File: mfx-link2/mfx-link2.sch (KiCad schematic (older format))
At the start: 48 parts, among them P1 CONN_01X04, P2 Gleisbox, P4 UART, P5 I2C, P6 CONN_02X03, P7 POTI, P8 IBT-2, Q1 BC817-40, T1 53040C, U1 6N137, U2 7805, U3 LM393, U4 78L05, U5 PIC16F1709

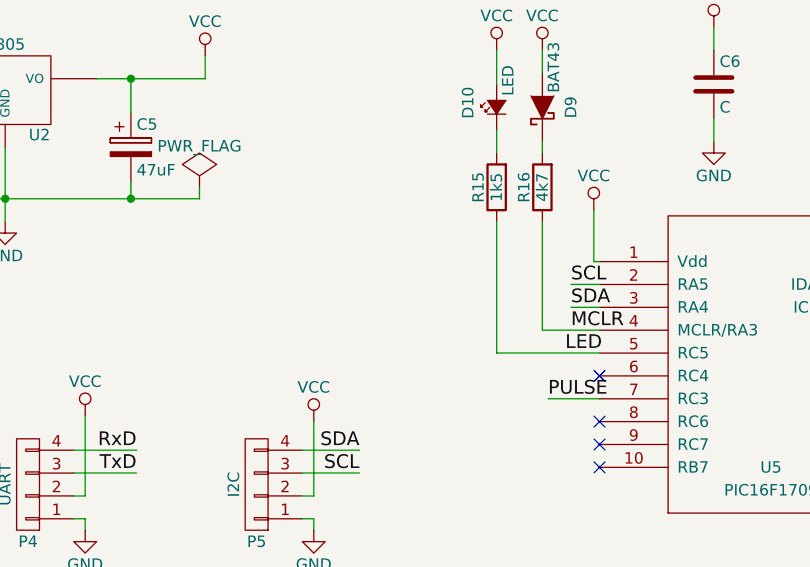
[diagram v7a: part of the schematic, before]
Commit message: add switch button
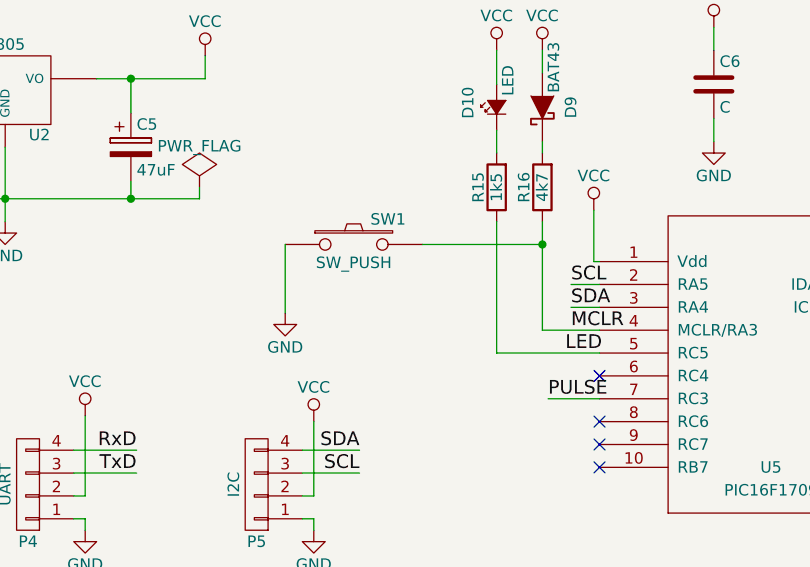
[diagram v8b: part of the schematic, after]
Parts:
- added SW1: SW_PUSH, w_switch:PCB_PUSH, symbol SW_PUSH
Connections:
- net GND: now also SW1.1
- net MCLR: now also SW1.2
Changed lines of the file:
@@
 EESchema Schematic File Version 2
+LIBS:mfx-link2-rescue
 LIBS:power
 LIBS:device
@@
 $EndComp
 $Comp
-L PWR_FLAG #FLG01
+L PWR_FLAG #FLG2
 U 1 1 58FE3ABA
 P 4950 1775
-F 0 "#FLG01" H 4950 1870 50  0001 C CNN
+F 0 "#FLG2" H 4950 1870 50  0001 C CNN
 F 1 "PWR_FLAG" H 4950 1955 50  0000 C CNN
 F 2 "" H 4950 1775 50  0000 C CNN
@@
 $EndComp
 $Comp
-L +5V #PWR02
+L +5V #PWR5
 U 1 1 58FE4D35
 P 3950 6350
-F 0 "#PWR02" H 3950 6200 50  0001 C CNN
+F 0 "#PWR5" H 3950 6200 50  0001 C CNN
 F 1 "+5V" H 3950 6490 50  0000 C CNN
 F 2 "" H 3950 6350 50  0000 C CNN
@@
 ENABLE
 $Comp
-L GND #PWR03
+L GND #PWR27
 U 1 1 58FE66BD
 P 10325 3075
-F 0 "#PWR03" H 10325 2825 50  0001 C CNN
+F 0 "#PWR27" H 10325 2825 50  0001 C CNN
 F 1 "GND" H 10325 2925 50  0000 C CNN
 F 2 "" H 10325 3075 50  0000 C CNN
@@
 SENSE
 $Comp
-L GND #PWR04
+L GND #PWR22
 U 1 1 58FE942D
 P 8475 2200
-F 0 "#PWR04" H 8475 1950 50  0001 C CNN
+F 0 "#PWR22" H 8475 1950 50  0001 C CNN
 F 1 "GND" H 8475 2050 50  0000 C CNN
 F 2 "" H 8475 2200 50  0000 C CNN
@@
 $EndComp
 $Comp
-L GND #PWR05
+L GND #PWR24
 U 1 1 58FFB153
 P 8750 1925
-F 0 "#PWR05" H 8750 1675 50  0001 C CNN
+F 0 "#PWR24" H 8750 1675 50  0001 C CNN
 F 1 "GND" H 8750 1775 50  0000 C CNN
 F 2 "" H 8750 1925 50  0000 C CNN
@@
 _GB_OUT
 $Comp
-L GNDA #PWR06
+L GNDA #PWR16
 U 1 1 59001DF4
 P 5625 7000
-F 0 "#PWR06" H 5625 6750 50  0001 C CNN
+F 0 "#PWR16" H 5625 6750 50  0001 C CNN
 F 1 "GNDA" H 5625 6850 50  0000 C CNN
 F 2 "" H 5625 7000 50  0000 C CNN
@@
 $EndComp
 $Comp
-L +5V #PWR07
+L +5V #PWR11
 U 1 1 5909C148
 P 4650 4825
-F 0 "#PWR07" H 4650 4675 50  0001 C CNN
+F 0 "#PWR11" H 4650 4675 50  0001 C CNN
 F 1 "+5V" H 4650 4965 50  0000 C CNN
 F 2 "" H 4650 4825 50  0000 C CNN
@@
 $EndComp
 $Comp
-L PWR_FLAG #FLG08
+L PWR_FLAG #FLG1
 U 1 1 590A0357
 P 3375 5550
-F 0 "#FLG08" H 3375 5645 50  0001 C CNN
+F 0 "#FLG1" H 3375 5645 50  0001 C CNN
 F 1 "PWR_FLAG" H 3375 5730 50  0000 C CNN
 F 2 "" H 3375 5550 50  0000 C CNN
@@
 red
 $Comp
-L +5V #PWR09
+L +5V #PWR3
 U 1 1 5908A86E
 P 3525 6075
-F 0 "#PWR09" H 3525 5925 50  0001 C CNN
+F 0 "#PWR3" H 3525 5925 50  0001 C CNN
 F 1 "+5V" H 3525 6215 50  0000 C CNN
 F 2 "" H 3525 6075 50  0000 C CNN
@@
 $EndComp
 $Comp
-L GND #PWR010
+L GND #PWR7
 U 1 1 58FE372A
 P 4100 1925
-F 0 "#PWR010" H 4100 1675 50  0001 C CNN
+F 0 "#PWR7" H 4100 1675 50  0001 C CNN
 F 1 "GND" H 4100 1775 50  0000 C CNN
 F 2 "" H 4100 1925 50  0000 C CNN
@@
 $EndComp
 $Comp
-L GND #PWR011
+L GND #PWR21
 U 1 1 58FE38A1
 P 7200 1575
-F 0 "#PWR011" H 7200 1325 50  0001 C CNN
+F 0 "#PWR21" H 7200 1325 50  0001 C CNN
 F 1 "GND" H 7200 1425 50  0000 C CNN
 F 2 "" H 7200 1575 50  0000 C CNN
@@
 $EndComp
 $Comp
-L GND #PWR012
+L GND #PWR15
 U 1 1 58FF775E
 P 5450 3275
-F 0 "#PWR012" H 5450 3025 50  0001 C CNN
+F 0 "#PWR15" H 5450 3025 50  0001 C CNN
 F 1 "GND" H 5450 3125 50  0000 C CNN
 F 2 "" H 5450 3275 50  0000 C CNN
@@
 $EndComp
 $Comp
-L GND #PWR013
+L GND #PWR10
 U 1 1 58FF8516
 P 4450 3275
-F 0 "#PWR013" H 4450 3025 50  0001 C CNN
+F 0 "#PWR10" H 4450 3025 50  0001 C CNN
 F 1 "GND" H 4450 3125 50  0000 C CNN
 F 2 "" H 4450 3275 50  0000 C CNN
@@
 $EndComp
 $Comp
-L GND #PWR014
+L GND #PWR2
 U 1 1 5909205E
 P 3100 3300
-F 0 "#PWR014" H 3100 3050 50  0001 C CNN
+F 0 "#PWR2" H 3100 3050 50  0001 C CNN
 F 1 "GND" H 3100 3150 50  0000 C CNN
 F 2 "" H 3100 3300 50  0000 C CNN
@@
 $EndComp
 $Comp
-L GNDA #PWR015
+L GNDA #PWR6
 U 1 1 59092D00
 P 3950 7150
-F 0 "#PWR015" H 3950 6900 50  0001 C CNN
+F 0 "#PWR6" H 3950 6900 50  0001 C CNN
 F 1 "GNDA" H 3950 7000 50  0000 C CNN
 F 2 "" H 3950 7150 50  0000 C CNN
@@
 $EndComp
 $Comp
-L GNDA #PWR016
+L GNDA #PWR4
 U 1 1 59092E5B
 P 3525 7425
-F 0 "#PWR016" H 3525 7175 50  0001 C CNN
+F 0 "#PWR4" H 3525 7175 50  0001 C CNN
 F 1 "GNDA" H 3525 7275 50  0000 C CNN
 F 2 "" H 3525 7425 50  0000 C CNN
@@
 $EndComp
 $Comp
-L GNDA #PWR017
+L GNDA #PWR8
 U 1 1 590931B4
 P 4150 5750
-F 0 "#PWR017" H 4150 5500 50  0001 C CNN
+F 0 "#PWR8" H 4150 5500 50  0001 C CNN
 F 1 "GNDA" H 4150 5600 50  0000 C CNN
 F 2 "" H 4150 5750 50  0000 C CNN
@@
 $EndComp
 $Comp
-L VCC #PWR018
+L VCC #PWR12
 U 1 1 59094284
 P 4975 1200
-F 0 "#PWR018" H 4975 1050 50  0001 C CNN
+F 0 "#PWR12" H 4975 1050 50  0001 C CNN
 F 1 "VCC" H 4975 1350 50  0000 C CNN
 F 2 "" H 4975 1200 50  0000 C CNN
@@
 $EndComp
 $Comp
-L VCC #PWR019
+L VCC #PWR20
 U 1 1 590943B0
 P 7200 1075
-F 0 "#PWR019" H 7200 925 50  0001 C CNN
+F 0 "#PWR20" H 7200 925 50  0001 C CNN
 F 1 "VCC" H 7200 1225 50  0000 C CNN
 F 2 "" H 7200 1075 50  0000 C CNN
@@
 $EndComp
 $Comp
-L VCC #PWR020
+L VCC #PWR17
 U 1 1 590944D7
 P 6250 1175
-F 0 "#PWR020" H 6250 1025 50  0001 C CNN
+F 0 "#PWR17" H 6250 1025 50  0001 C CNN
 F 1 "VCC" H 6250 1325 50  0000 C CNN
 F 2 "" H 6250 1175 50  0000 C CNN
@@
 $EndComp
 $Comp
-L VCC #PWR021
+L VCC #PWR18
 U 1 1 5909459E
 P 6450 1175
-F 0 "#PWR021" H 6450 1025 50  0001 C CNN
+F 0 "#PWR18" H 6450 1025 50  0001 C CNN
 F 1 "VCC" H 6450 1325 50  0000 C CNN
 F 2 "" H 6450 1175 50  0000 C CNN
@@
 $EndComp
 $Comp
-L VCC #PWR022
+L VCC #PWR19
 U 1 1 5909516C
 P 6675 1875
-F 0 "#PWR022" H 6675 1725 50  0001 C CNN
+F 0 "#PWR19" H 6675 1725 50  0001 C CNN
 F 1 "VCC" H 6675 2025 50  0000 C CNN
 F 2 "" H 6675 1875 50  0000 C CNN
@@
 $EndComp
 $Comp
-L VCC #PWR023
+L VCC #PWR1
 U 1 1 5909A87E
 P 3000 2425
-F 0 "#PWR023" H 3000 2275 50  0001 C CNN
+F 0 "#PWR1" H 3000 2275 50  0001 C CNN
 F 1 "VCC" H 3000 2575 50  0000 C CNN
 F 2 "" H 3000 2425 50  0000 C CNN
@@
 $EndComp
 $Comp
-L VCC #PWR024
+L VCC #PWR14
 U 1 1 5909D6E9
 P 5450 2800
-F 0 "#PWR024" H 5450 2650 50  0001 C CNN
+F 0 "#PWR14" H 5450 2650 50  0001 C CNN
 F 1 "VCC" H 5450 2950 50  0000 C CNN
 F 2 "" H 5450 2800 50  0000 C CNN
@@
 $EndComp
 $Comp
-L VCC #PWR025
+L VCC #PWR9
 U 1 1 5909D844
 P 4450 2775
-F 0 "#PWR025" H 4450 2625 50  0001 C CNN
+F 0 "#PWR9" H 4450 2625 50  0001 C CNN
 F 1 "VCC" H 4450 2925 50  0000 C CNN
 F 2 "" H 4450 2775 50  0000 C CNN
@@
 	4650 1450 4650 1300
 $Comp
-L VCC #PWR026
+L VCC #PWR23
 U 1 1 590A14EA
 P 8750 1425
-F 0 "#PWR026" H 8750 1275 50  0001 C CNN
+F 0 "#PWR23" H 8750 1275 50  0001 C CNN
 F 1 "VCC" H 8750 1575 50  0000 C CNN
 F 2 "" H 8750 1425 50  0000 C CNN
@@
 $EndComp
 $Comp
-L VCC #PWR027
+L VCC #PWR26
 U 1 1 590A1627
 P 10200 1775
-F 0 "#PWR027" H 10200 1625 50  0001 C CNN
+F 0 "#PWR26" H 10200 1625 50  0001 C CNN
 F 1 "VCC" H 10200 1925 50  0000 C CNN
 F 2 "" H 10200 1775 50  0000 C CNN
@@
 $EndComp
 $Comp
-L VCC #PWR028
+L VCC #PWR25
 U 1 1 590A3FCB
 P 9400 2250
-F 0 "#PWR028" H 9400 2100 50  0001 C CNN
+F 0 "#PWR25" H 9400 2100 50  0001 C CNN
 F 1 "VCC" H 9400 2400 50  0000 C CNN
 F 2 "" H 9400 2250 50  0000 C CNN
@@
 Text Label 4575 5150 2    60   ~ 0
 VO
+$Comp
+L SW_PUSH SW1
+U 1 1 59358361
+P 5625 2025
+F 0 "SW1" H 5775 2135 50  0000 C CNN
+F 1 "SW_PUSH" H 5625 1945 50  0000 C CNN
+F 2 "w_switch:PCB_PUSH" H 5625 2025 50  0001 C CNN
+F 3 "" H 5625 2025 50  0000 C CNN
+	1    5625 2025
+	1    0    0    -1
+$EndComp
+Wire Wire Line
+	6450 2025 5925 2025
+Connection ~ 6450 2025
+Wire Wire Line
+	5325 2025 5325 2325
+$Comp
+L GND #PWR13
+U 1 1 59358A73
+P 5325 2325
+F 0 "#PWR13" H 5325 2075 50  0001 C CNN
+F 1 "GND" H 5325 2175 50  0000 C CNN
+F 2 "" H 5325 2325 50  0000 C CNN
+F 3 "" H 5325 2325 50  0000 C CNN
+	1    5325 2325
+	1    0    0    -1
+$EndComp
 $EndSCHEMATC
